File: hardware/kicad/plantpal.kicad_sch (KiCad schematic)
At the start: 0 parts

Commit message: wip: revision 2
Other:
- sheet Main Controller ports: added MPP_STATUS; removed none
- sheet Solar Power ports: added MPP_STATUS; removed none
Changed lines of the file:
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@@
     (rev "2")
   )
-  (junction (at 149.225 77.47) (diameter 0) (color 0 0 0 0)
+  (junction (at 148.59 77.47) (diameter 0) (color 0 0 0 0)
   )
   (junction (at 93.345 82.55) (diameter 0) (color 0 0 0 0)
   )
-  (wire (pts (xy 149.225 77.47) (xy 158.75 77.47))
+  (wire (pts (xy 148.59 77.47) (xy 146.05 77.47))
+    (stroke (width 0) (type default))
+  )
+  (wire (pts (xy 93.345 62.865) (xy 93.345 82.55))
     (stroke (width 0) (type default))
   )
@@
     (stroke (width 0) (type default))
   )
+  (wire (pts (xy 151.765 56.515) (xy 151.765 76.835))
+    (stroke (width 0) (type default))
+  )
   (wire (pts (xy 196.215 111.76) (xy 214.63 111.76))
     (stroke (width 0) (type default))
   )
+  (wire (pts (xy 158.75 80.01) (xy 148.59 80.01))
+    (stroke (width 0) (type default))
+  )
+  (wire (pts (xy 148.59 77.47) (xy 148.59 75.565))
+    (stroke (width 0) (type default))
+  )
   (wire (pts (xy 214.63 73.025) (xy 210.185 73.025))
     (stroke (width 0) (type default))
@@
     (stroke (width 0) (type default))
   )
-  (wire (pts (xy 99.06 56.515) (xy 99.06 78.74))
-    (stroke (width 0) (type default))
-  )
   (wire (pts (xy 154.94 73.66) (xy 158.75 73.66))
     (stroke (width 0) (type default))
@@
     (stroke (width 0) (type default))
   )
-  (wire (pts (xy 93.345 62.23) (xy 93.345 82.55))
-    (stroke (width 0) (type default))
-  )
   (wire (pts (xy 196.215 82.55) (xy 214.63 82.55))
     (stroke (width 0) (type default))
@@
     (stroke (width 0) (type default))
   )
+  (wire (pts (xy 151.765 76.835) (xy 158.75 76.835))
+    (stroke (width 0) (type default))
+  )
   (wire (pts (xy 99.06 78.74) (xy 103.505 78.74))
     (stroke (width 0) (type default))
   )
-  (wire (pts (xy 82.55 62.23) (xy 93.345 62.23))
-    (stroke (width 0) (type default))
-  )
   (wire (pts (xy 82.55 53.34) (xy 154.94 53.34))
     (stroke (width 0) (type default))
@@
     (stroke (width 0) (type default))
   )
+  (wire (pts (xy 99.06 59.69) (xy 99.06 78.74))
+    (stroke (width 0) (type default))
+  )
+  (wire (pts (xy 148.59 80.01) (xy 148.59 77.47))
+    (stroke (width 0) (type default))
+  )
   (wire (pts (xy 196.215 91.44) (xy 214.63 91.44))
     (stroke (width 0) (type default))
@@
     (stroke (width 0) (type default))
   )
-  (wire (pts (xy 146.05 77.47) (xy 149.225 77.47))
-    (stroke (width 0) (type default))
-  )
-  (wire (pts (xy 149.225 71.755) (xy 149.225 77.47))
-    (stroke (width 0) (type default))
-  )
-  (wire (pts (xy 82.55 56.515) (xy 99.06 56.515))
+  (wire (pts (xy 82.55 56.515) (xy 151.765 56.515))
+    (stroke (width 0) (type default))
+  )
+  (wire (pts (xy 82.55 62.865) (xy 93.345 62.865))
+    (stroke (width 0) (type default))
+  )
+  (wire (pts (xy 82.55 59.69) (xy 99.06 59.69))
     (stroke (width 0) (type default))
   )
@@
     )
   )
-  (symbol (lib_id "power:+3V3") (at 149.225 71.755 0) (unit 1)
+  (symbol (lib_id "power:+3V3") (at 148.59 75.565 0) (unit 1)
     (in_bom yes) (on_board yes) (dnp no)
-    (property "Reference" "#PWR01" (at 149.225 75.565 0)
-      (effects (font (size 1.27 1.27)) hide)
-    )
-    (property "Value" "+3V3" (at 150.495 67.945 0)
-      (effects (font (size 1.27 1.27)) (justify right))
-    )
-    (property "Footprint" "" (at 149.225 71.755 0)
-      (effects (font (size 1.27 1.27)) hide)
-    )
-    (property "Datasheet" "" (at 149.225 71.755 0)
+    (property "Reference" "#PWR062" (at 148.59 79.375 0)
+      (effects (font (size 1.27 1.27)) hide)
+    )
+    (property "Value" "+3V3" (at 149.86 71.755 0)
+      (effects (font (size 1.27 1.27)) (justify right))
+    )
+    (property "Footprint" "" (at 148.59 75.565 0)
+      (effects (font (size 1.27 1.27)) hide)
+    )
+    (property "Datasheet" "" (at 148.59 75.565 0)
       (effects (font (size 1.27 1.27)) hide)
     )
@@
       (project "plantpal"
         (path "/59b4123e-c7be-466b-a5db-658b8f0c1171"
-          (reference "#PWR01") (unit 1)
+          (reference "#PWR062") (unit 1)
         )
         (path "/59b4123e-c7be-466b-a5db-658b8f0c1171/416559aa-55f3-4db2-bf13-04c2bb6b0caa"
@@
     )
   )
-  (sheet (at 55.245 50.8) (size 27.305 13.97) (fields_autoplaced)
+  (sheet (at 55.245 50.8) (size 27.305 14.605) (fields_autoplaced)
     (stroke (width 0.1524) (type solid))
     (fill (color 0 0 0 0.0000))
@@
       (effects (font (size 1.27 1.27)) (justify left bottom))
     )
-    (property "Sheetfile" "solar_power.kicad_sch" (at 55.245 65.3546 0)
-      (effects (font (size 1.27 1.27)) (justify left top))
-    )
-    (pin "LDO_EN" output (at 82.55 56.515 0)
+    (property "Sheetfile" "solar_power.kicad_sch" (at 55.245 65.9896 0)
+      (effects (font (size 1.27 1.27)) (justify left top))
+    )
+    (pin "LDO_EN" output (at 82.55 59.69 0)
       (effects (font (size 1.27 1.27)) (justify right))
     )
@@
       (effects (font (size 1.27 1.27)) (justify right))
     )
-    (pin "+BATT" bidirectional (at 82.55 62.23 0)
+    (pin "+BATT" bidirectional (at 82.55 62.865 0)
+      (effects (font (size 1.27 1.27)) (justify right))
+    )
+    (pin "MPP_STATUS" output (at 82.55 56.515 0)
       (effects (font (size 1.27 1.27)) (justify right))
     )
@@
       (effects (font (size 1.27 1.27)) (justify left))
     )
-    (pin "+3V3" input (at 158.75 77.47 180)
+    (pin "+3V3" input (at 158.75 80.01 180)
       (effects (font (size 1.27 1.27)) (justify left))
     )
@@
       (effects (font (size 1.27 1.27)) (justify right))
     )
-    (instances
+    (pin "MPP_STATUS" input (at 158.75 76.835 180)
+      (effects (font (size 1.27 1.27)) (justify left))
+    )
+    (instances

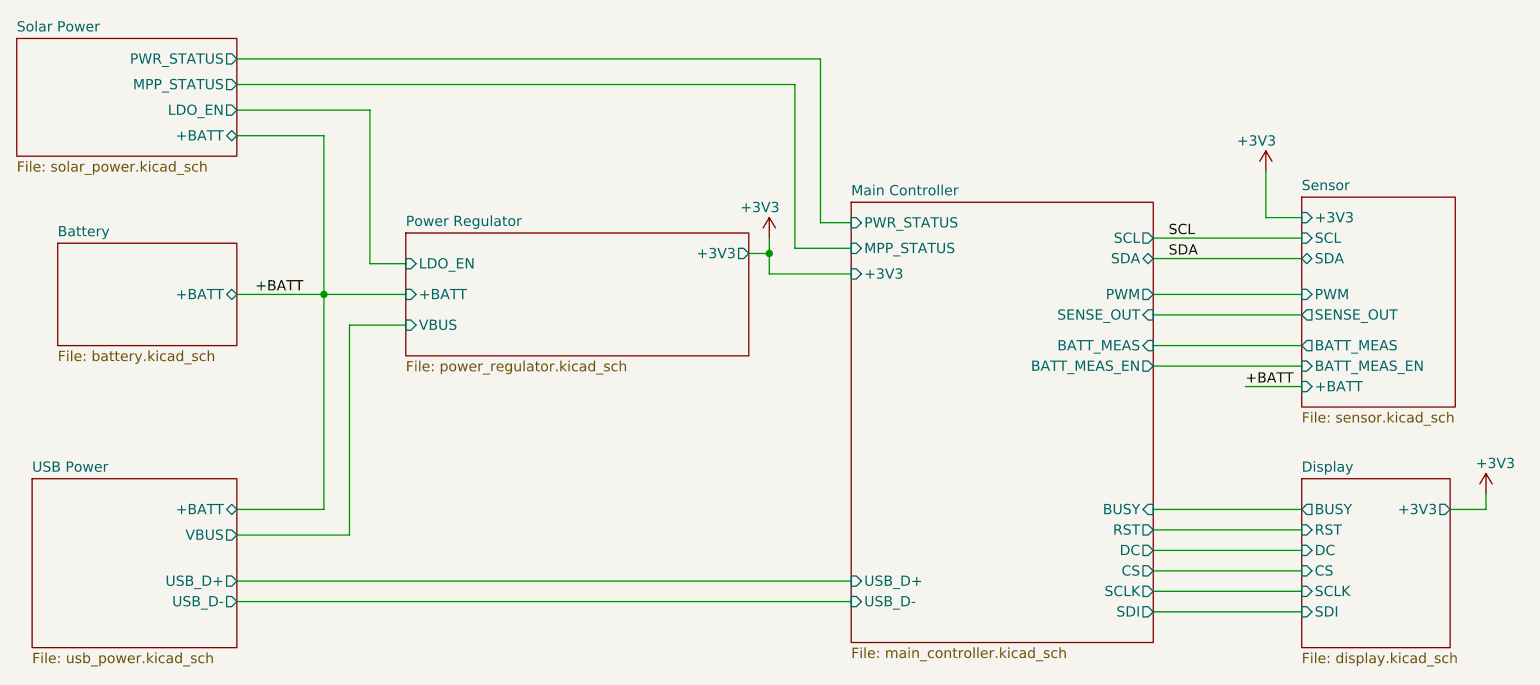
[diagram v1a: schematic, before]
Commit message: re-route sense out, add display power switch
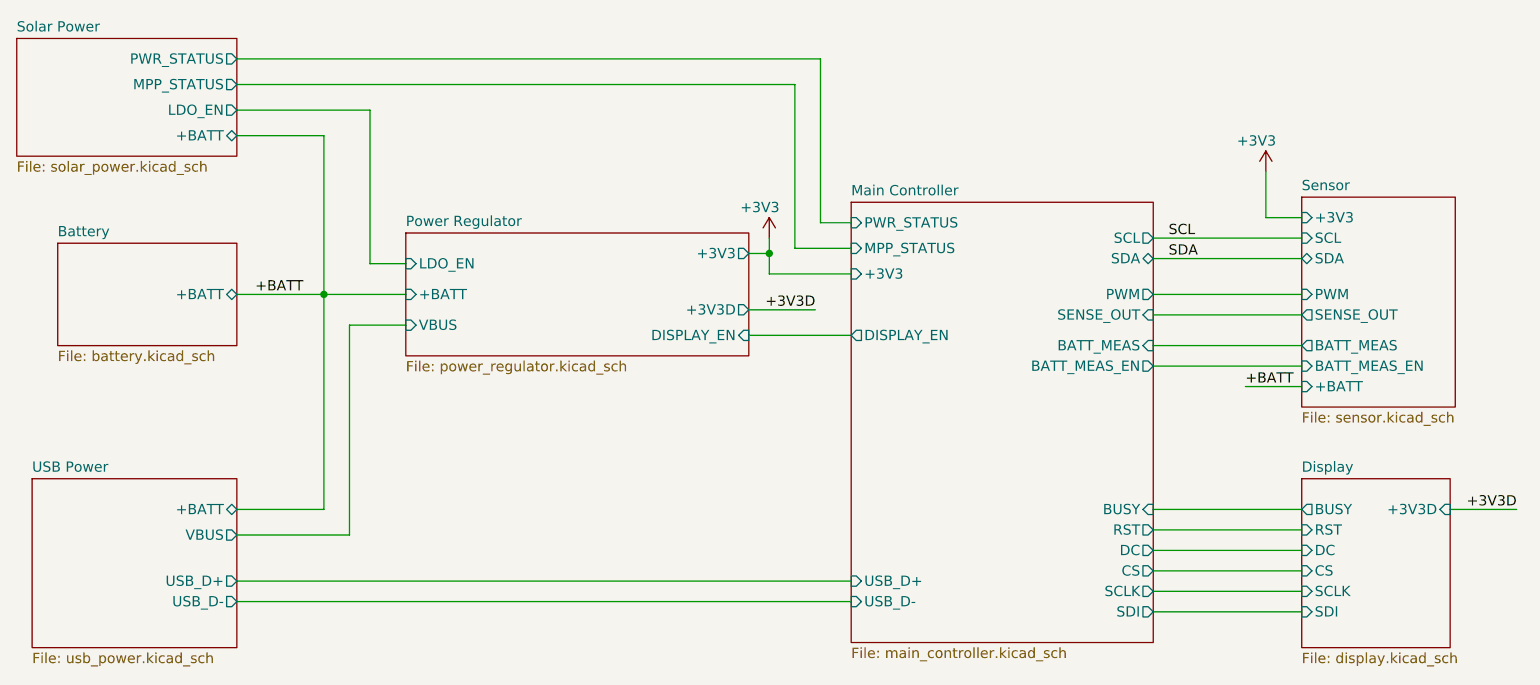
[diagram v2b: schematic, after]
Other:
- sheet Display ports: added +3V3D; removed +3V3
- sheet Main Controller ports: added DISPLAY_EN; removed none
- sheet Power Regulator ports: added +3V3D, DISPLAY_EN; removed none
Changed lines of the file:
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@@
     (stroke (width 0) (type default))
   )
-  (wire (pts (xy 233.045 109.22) (xy 237.49 109.22))
+  (wire (pts (xy 233.045 109.22) (xy 241.3 109.22))
     (stroke (width 0) (type default))
   )
@@
     (stroke (width 0) (type default))
   )
+  (wire (pts (xy 146.05 84.455) (xy 154.305 84.455))
+    (stroke (width 0) (type default))
+  )
   (wire (pts (xy 207.645 93.98) (xy 214.63 93.98))
     (stroke (width 0) (type default))
@@
     (stroke (width 0) (type default))
   )
-  (wire (pts (xy 237.49 109.22) (xy 237.49 107.315))
-    (stroke (width 0) (type default))
-  )
   (wire (pts (xy 196.215 121.92) (xy 214.63 121.92))
     (stroke (width 0) (type default))
   )
+  (wire (pts (xy 146.05 87.63) (xy 158.75 87.63))
+    (stroke (width 0) (type default))
+  )
   (wire (pts (xy 82.55 109.22) (xy 93.345 109.22))
     (stroke (width 0) (type default))
@@
   (wire (pts (xy 82.55 118.11) (xy 158.75 118.11))
     (stroke (width 0) (type default))
+  )
+  (label "+3V3D" (at 154.305 84.455 180) (fields_autoplaced)
+    (effects (font (size 1.27 1.27)) (justify right bottom))
+  )
+  (label "+3V3D" (at 241.3 109.22 180) (fields_autoplaced)
+    (effects (font (size 1.27 1.27)) (justify right bottom))
   )
   (label "SDA" (at 198.12 78.105 0) (fields_autoplaced)
@@
     (effects (font (size 1.27 1.27)) (justify left bottom))
   )
-  (symbol (lib_id "power:+3V3") (at 237.49 107.315 0) (mirror y) (unit 1)
+  (symbol (lib_id "power:+3V3") (at 210.185 67.31 0) (unit 1)
     (in_bom yes) (on_board yes) (dnp no)
-    (property "Reference" "#PWR03" (at 237.49 111.125 0)
-      (effects (font (size 1.27 1.27)) hide)
-    )
-    (property "Value" "+3V3" (at 236.22 103.505 0)
-      (effects (font (size 1.27 1.27)) (justify right))
-    )
-    (property "Footprint" "" (at 237.49 107.315 0)
-      (effects (font (size 1.27 1.27)) hide)
-    )
-    (property "Datasheet" "" (at 237.49 107.315 0)
+    (property "Reference" "#PWR02" (at 210.185 71.12 0)
+      (effects (font (size 1.27 1.27)) hide)
+    )
+    (property "Value" "+3V3" (at 211.455 63.5 0)
+      (effects (font (size 1.27 1.27)) (justify right))
+    )
+    (property "Footprint" "" (at 210.185 67.31 0)
+      (effects (font (size 1.27 1.27)) hide)
+    )
+    (property "Datasheet" "" (at 210.185 67.31 0)
       (effects (font (size 1.27 1.27)) hide)
     )
@@
       (project "plantpal"
         (path "/59b4123e-c7be-466b-a5db-658b8f0c1171"
-          (reference "#PWR03") (unit 1)
+          (reference "#PWR02") (unit 1)
         )
         (path "/59b4123e-c7be-466b-a5db-658b8f0c1171/416559aa-55f3-4db2-bf13-04c2bb6b0caa"
@@
     )
   )
-  (symbol (lib_id "power:+3V3") (at 210.185 67.31 0) (unit 1)
+  (symbol (lib_id "power:+3V3") (at 148.59 75.565 0) (unit 1)
     (in_bom yes) (on_board yes) (dnp no)
-    (property "Reference" "#PWR02" (at 210.185 71.12 0)
-      (effects (font (size 1.27 1.27)) hide)
-    )
-    (property "Value" "+3V3" (at 211.455 63.5 0)
-      (effects (font (size 1.27 1.27)) (justify right))
-    )
-    (property "Footprint" "" (at 210.185 67.31 0)
-      (effects (font (size 1.27 1.27)) hide)
-    )
-    (property "Datasheet" "" (at 210.185 67.31 0)
+    (property "Reference" "#PWR062" (at 148.59 79.375 0)
+      (effects (font (size 1.27 1.27)) hide)
+    )
+    (property "Value" "+3V3" (at 149.86 71.755 0)
+      (effects (font (size 1.27 1.27)) (justify right))
+    )
+    (property "Footprint" "" (at 148.59 75.565 0)
+      (effects (font (size 1.27 1.27)) hide)
+    )
+    (property "Datasheet" "" (at 148.59 75.565 0)
       (effects (font (size 1.27 1.27)) hide)
     )
@@
       (project "plantpal"
         (path "/59b4123e-c7be-466b-a5db-658b8f0c1171"
-          (reference "#PWR02") (unit 1)
+          (reference "#PWR062") (unit 1)
         )
         (path "/59b4123e-c7be-466b-a5db-658b8f0c1171/416559aa-55f3-4db2-bf13-04c2bb6b0caa"
@@
     )
   )
-  (symbol (lib_id "power:+3V3") (at 148.59 75.565 0) (unit 1)
-    (in_bom yes) (on_board yes) (dnp no)
-    (property "Reference" "#PWR062" (at 148.59 79.375 0)
-      (effects (font (size 1.27 1.27)) hide)
-    )
-    (property "Value" "+3V3" (at 149.86 71.755 0)
-      (effects (font (size 1.27 1.27)) (justify right))
-    )
-    (property "Footprint" "" (at 148.59 75.565 0)
-      (effects (font (size 1.27 1.27)) hide)
-    )
-    (property "Datasheet" "" (at 148.59 75.565 0)
-      (effects (font (size 1.27 1.27)) hide)
-    )
-    (pin "1")
-    (instances
-      (project "plantpal"
-        (path "/59b4123e-c7be-466b-a5db-658b8f0c1171"
-          (reference "#PWR062") (unit 1)
-        )
-        (path "/59b4123e-c7be-466b-a5db-658b8f0c1171/416559aa-55f3-4db2-bf13-04c2bb6b0caa"
-          (reference "#PWR076") (unit 1)
-        )
-      )
-      (project "bwlr1e"
-        (path "/630c8da6-5464-4eef-824d-89618087f4b4"
-          (reference "#PWR0103") (unit 1)
-        )
-      )
-    )
-  )
   (sheet (at 103.505 74.93) (size 42.545 15.24) (fields_autoplaced)
     (stroke (width 0.1524) (type solid))
@@
       (effects (font (size 1.27 1.27)) (justify right))
     )
+    (pin "DISPLAY_EN" input (at 146.05 87.63 0)
+      (effects (font (size 1.27 1.27)) (justify right))
+    )
+    (pin "+3V3D" output (at 146.05 84.455 0)
+      (effects (font (size 1.27 1.27)) (justify right))
+    )
     (instances
       (project "plantpal"
@@
       (effects (font (size 1.27 1.27)) (justify left))
     )
-    (pin "+3V3" output (at 233.045 109.22 0)
+    (pin "+3V3D" input (at 233.045 109.22 0)
       (effects (font (size 1.27 1.27)) (justify right))
     )
@@
       (effects (font (size 1.27 1.27)) (justify left))
     )
+    (pin "DISPLAY_EN" output (at 158.75 87.63 180)
+      (effects (font (size 1.27 1.27)) (justify left))
+    )
